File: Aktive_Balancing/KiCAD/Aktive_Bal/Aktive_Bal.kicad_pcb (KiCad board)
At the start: 4 copper layers, 149 x 144 mm, 219 parts, among them J1 Screw_Terminal_01x02, J10 Conn_01x02_Pin, J11 Conn_01x02_Pin, J12 Conn_01x02_Pin, J13 Conn_01x02_Pin, J14 Conn_01x02_Pin, J15 Screw_Terminal_01x03, J16 Screw_Terminal_01x03, J17 Screw_Terminal_01x03, J18 Screw_Terminal_01x03, J19 Screw_Terminal_01x03, J2 A-DF_09_A_KG-T4S, J20 Screw_Terminal_01x03, J21 Conn_01x02_Pin, J22 Conn_01x02_Pin, J23 Conn_01x02_Pin, J24 Conn_01x02_Pin, J3 Conn_01x02_Pin, J4 Conn_01x02_Pin, J5 Conn_01x02_Pin, J6 Conn_01x02_Pin, J7 Sockel_BluePill, J9 Conn_01x02_Pin, Q1 BSS316NH6327XTSA1, Q10_H1 NTTFS6H888NL, Q10_L1 NTTFS6H888NL, Q11_H1 NTTFS6H888NL, Q11_L1 NTTFS6H888NL, Q12_H1 NTTFS6H888NL, Q12_L1 NTTFS6H888NL, Q13_H1 NTTFS6H888NL, Q13_L1 NTTFS6H888NL, Q14_H1 NTTFS6H888NL, Q14_L1 NTTFS6H888NL, Q15_H1 NTTFS6H888NL, Q15_L1 NTTFS6H888NL, Q16_H1 NTTFS6H888NL, Q16_L1 NTTFS6H888NL, Q1_H1 NTTFS6H888NL, Q1_L1 NTTFS6H888NL, Q2_H1 NTTFS6H888NL, Q2_L1 NTTFS6H888NL, Q3_H1 NTTFS6H888NL, Q3_L1 NTTFS6H888NL, Q4_H1 NTTFS6H888NL, Q4_L1 NTTFS6H888NL, Q5_H1 NTTFS6H888NL, Q5_L1 NTTFS6H888NL, Q6_H1 NTTFS6H888NL, Q6_L1 NTTFS6H888NL, Q7_H1 NTTFS6H888NL, Q7_L1 NTTFS6H888NL, Q8_H1 NTTFS6H888NL, Q8_L1 NTTFS6H888NL, Q9_H1 NTTFS6H888NL, Q9_L1 NTTFS6H888NL, U1 RFP12N10L, U10 LTV-847S, U11 LTV-847S, U12 LTV-847S, U13 LTV-847S, U14 TL084, U15 LM2596S-ADJ, U2 ADUM1250ARZ-RL7, U3 SN65HVD233, U4 SCW20C-12, U5 EC1SA16N, U6 PCA9306DC, U7 PCF8575CDB, U8 LM1117MP-3.3, U9 MCP4725xxx-xCH

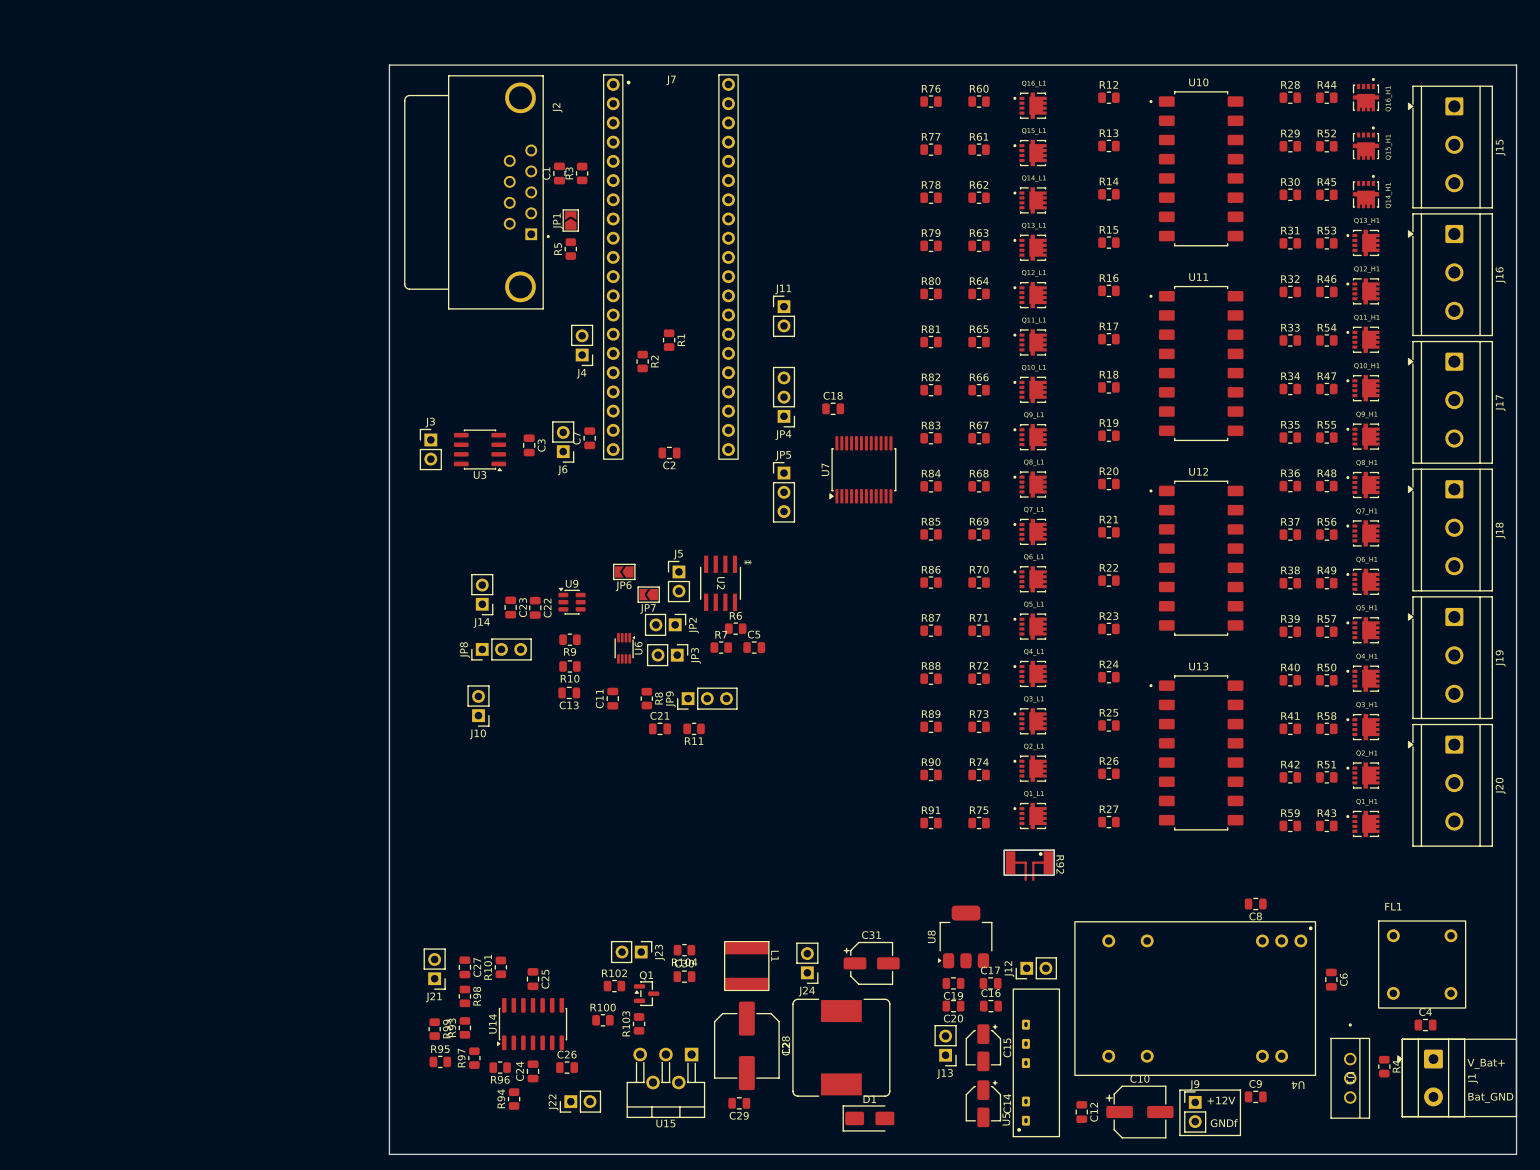
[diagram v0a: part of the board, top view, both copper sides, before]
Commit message: Layout kompakter gemacht
Ich habe die Sektion mit dem Mosfets gemacht. Weber hat es nicht anders gewollt...
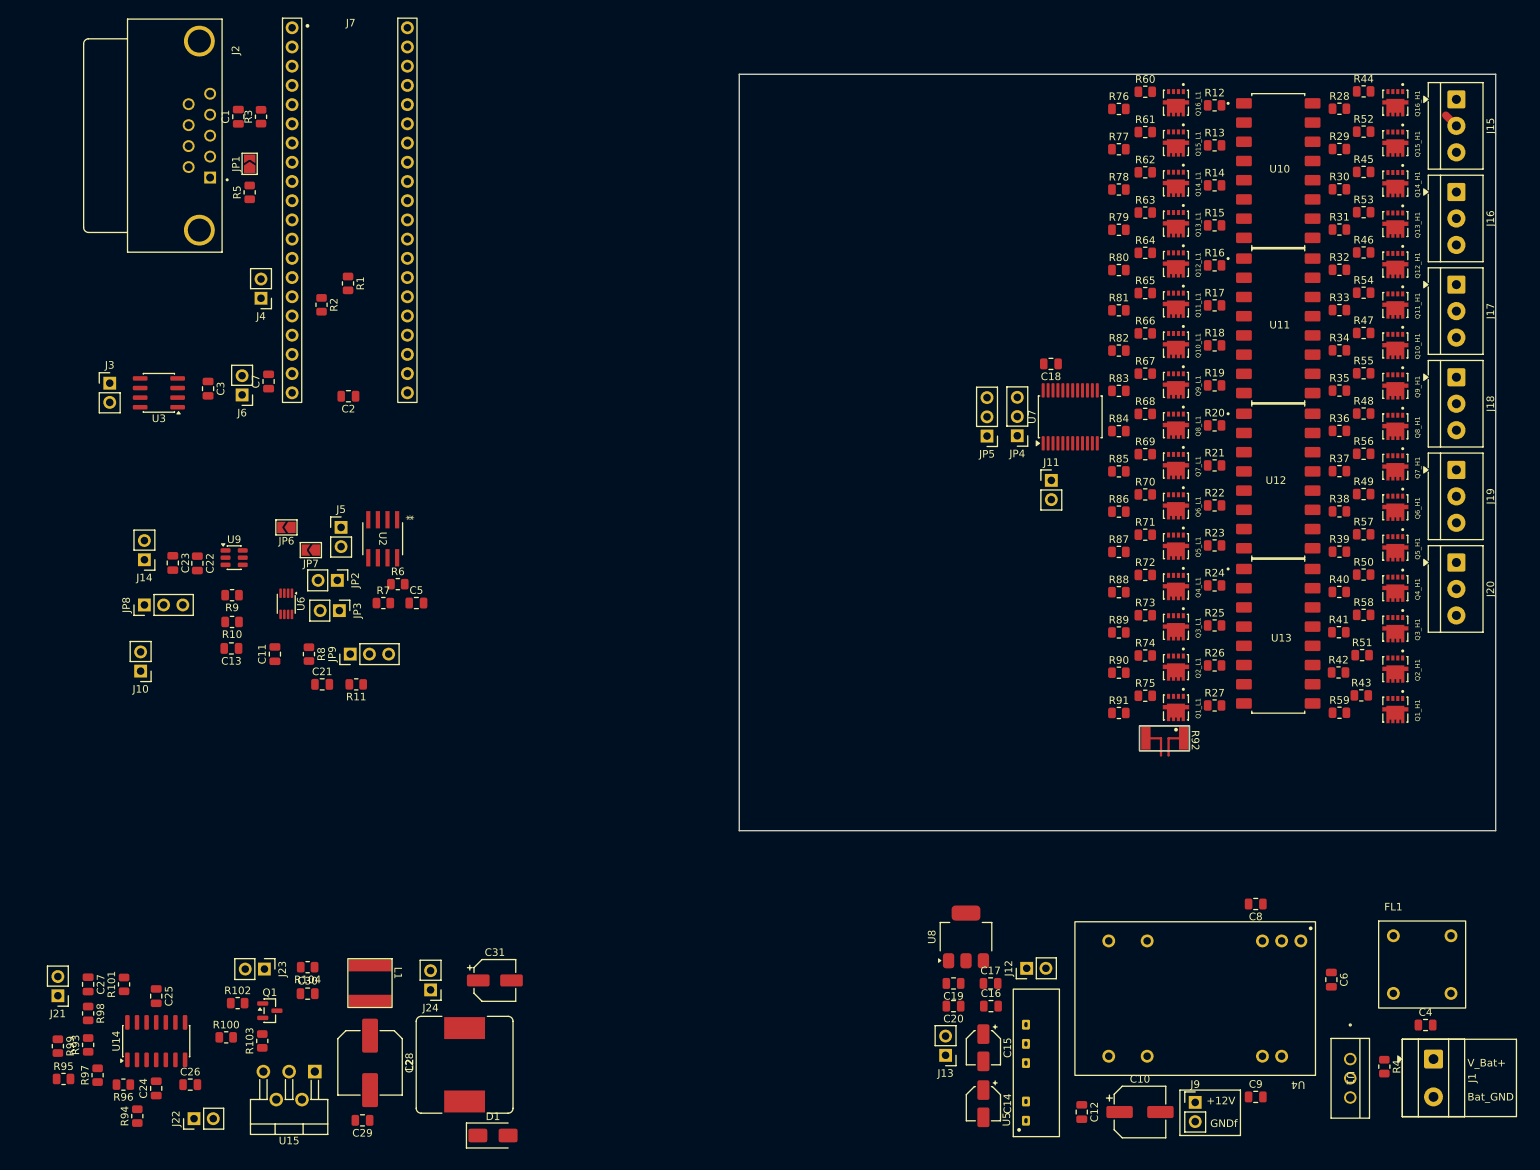
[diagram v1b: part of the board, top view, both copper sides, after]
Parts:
- J15, J16, J17, J18, J19, J20: footprint TerminalBlock_CUI:TerminalBlock_CUI_TB007-508-03_1x03_P5.08mm_Horizontal -> TerminalBlock_4Ucon:TerminalBlock_4Ucon_1x03_P3.50mm_Horizontal
- moved C25 49.9 mm to (59.2, 141.1)
- moved C29 49.9 mm to (86.4, 157.5)
- moved C30 49.9 mm to (79.2, 140.8)
- moved C31 49.9 mm to (103.9, 139.0)
- moved D1 49.9 mm to (103.7, 159.5)
- moved J23 49.9 mm to (73.5, 137.5)
- moved J24 49.9 mm to (95.4, 140.3)
- moved L1 49.9 mm to (87.4, 137.0)
- moved Q1 49.9 mm to (74.2, 143.0)
- moved R102 49.9 mm to (69.9, 142.0)
- moved R103 49.9 mm to (73.2, 147.0)
- moved R104 49.9 mm to (79.2, 137.3)
- moved R94 49.9 mm to (56.7, 156.9)
- moved R99 49.9 mm to (46.2, 147.7)
- moved C24 49.9 mm to (59.2, 153.3)
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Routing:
- net Cell15: track 0.00 -> 1.98 mm
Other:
- board size 149 x 144 mm -> 100 x 100 mm
- board text removed: "Port Expander"

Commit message: hassplatine
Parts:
- moved J10 141.2 mm to (177.0, 23.5)
- moved J14 137.2 mm to (181.0, 23.5)
- moved JP8 131.6 mm to (173.0, 26.0), turned to 180 degrees
- moved C23 127.9 mm to (176.9, 29.0), turned to 180 degrees
- moved C22 123.5 mm to (176.9, 32.5), turned to 180 degrees
- moved R9 117.6 mm to (172.0, 31.0), turned to 90 degrees
- moved U9 116.3 mm to (176.5, 37.5), turned to -90 degrees
- moved R10 116.3 mm to (168.5, 31.0), turned to 90 degrees
- moved C13 115.4 mm to (165.0, 30.9), turned to 90 degrees
- moved J22 113.5 mm to (154.5, 88.5)
- moved U15 110.9 mm to (168.5, 84.0)
- moved JP6 110.2 mm to (179.9, 41.4), turned to 90 degrees
- moved R94 109.9 mm to (143.4, 89.5), turned to 180 degrees
- moved C24 109.5 mm to (146.0, 86.5)
- moved C25 109.5 mm to (146.0, 74.3)
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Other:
- board size 100 x 100 mm -> 108.8 x 101 mm
- board text removed: "+12V"
- board text removed: "Bat_GND"
- board text removed: "CAN-Anbindung mit Sub-D-Stecker, Tranceiver, STM32"
- board text removed: "GNDf"
- board text removed: "I2C-Kram"
- board text removed: "Leistungsmosfets"
- board text removed: "OPV mit Regelkreis"
- board text removed: "Spannungsversorgungen"
- board text removed: "V_Bat+"

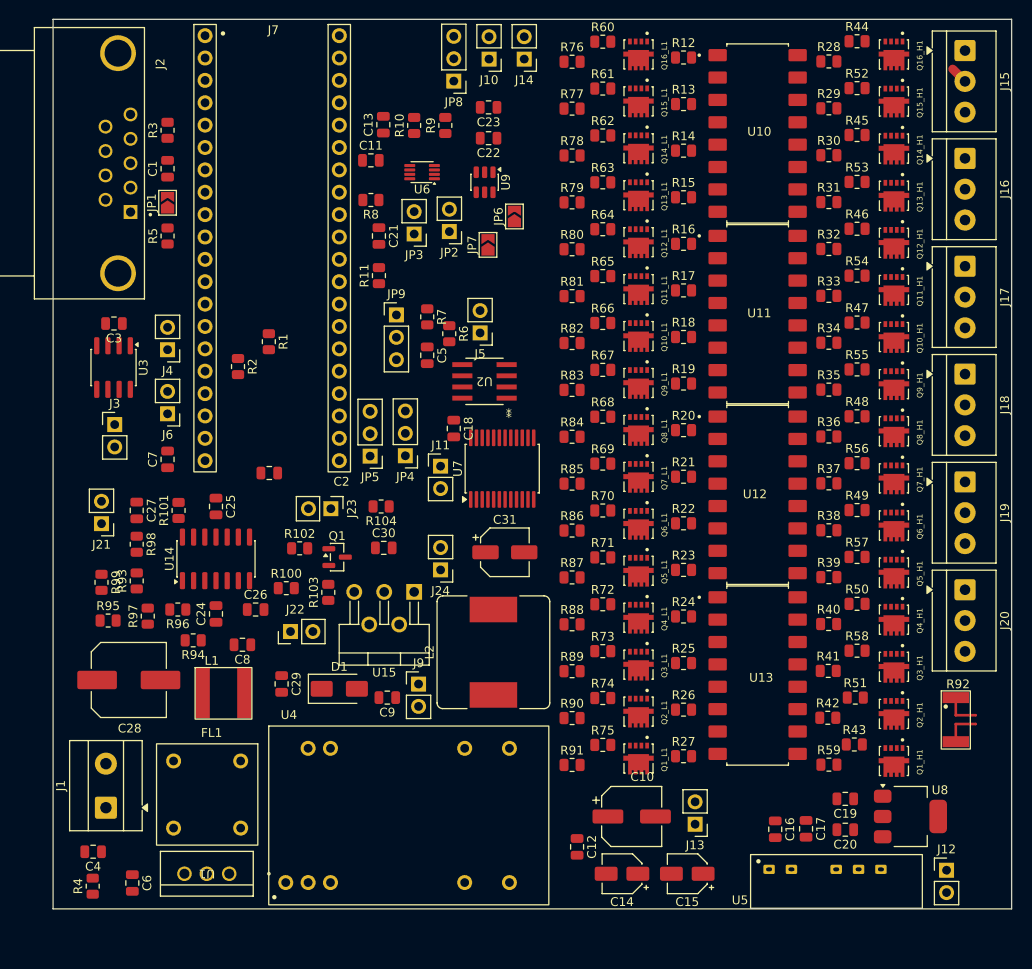
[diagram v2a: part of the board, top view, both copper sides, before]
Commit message: Microcontroller geroutet
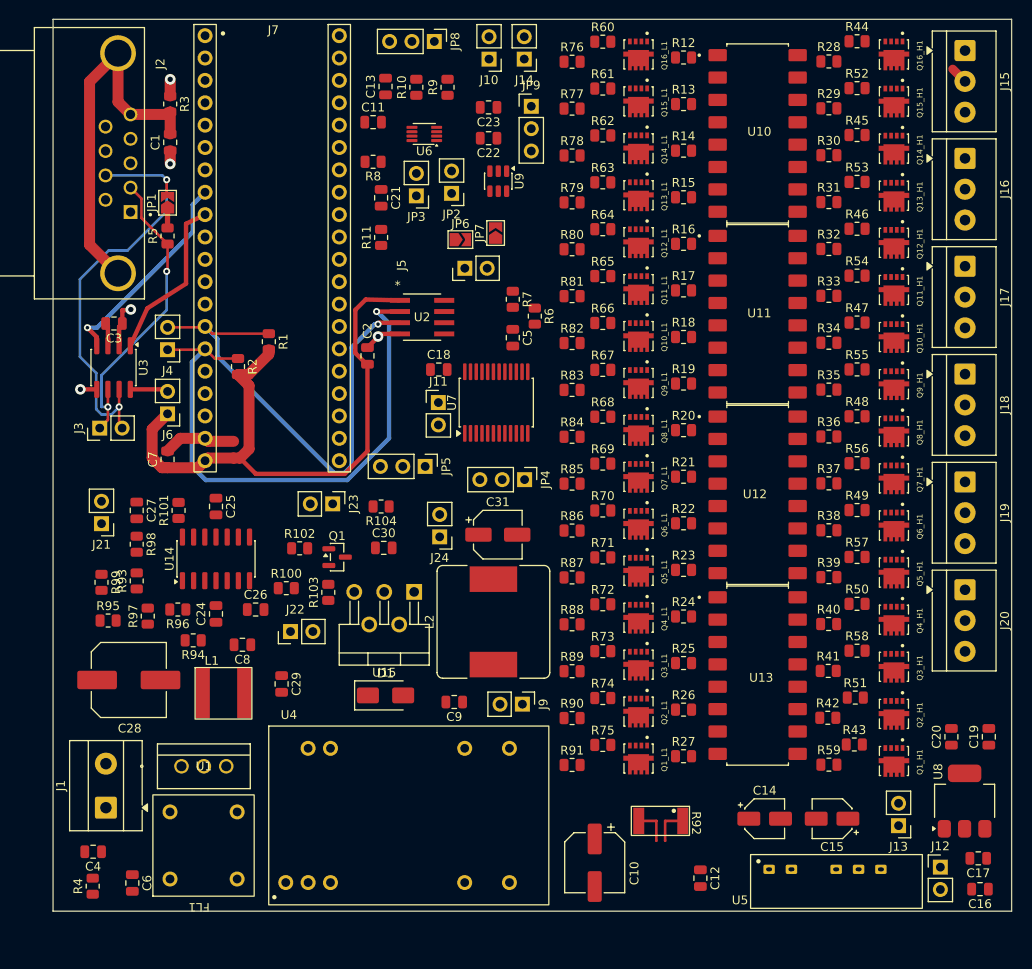
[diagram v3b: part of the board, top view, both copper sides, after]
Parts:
- moved R92 34.0 mm to (199.0, 110.0), turned to -90 degrees
- moved JP9 28.2 mm to (181.8, 28.9)
- moved C16 24.2 mm to (232.8, 117.8), turned to 180 degrees
- moved J13 23.1 mm to (223.5, 110.5)
- moved C17 19.8 mm to (232.6, 114.2), turned to 180 degrees
- moved C19 17.8 mm to (233.8, 100.5), turned to 90 degrees
- moved C15 17.6 mm to (215.9, 109.8)
- moved C14 17.4 mm to (208.3, 109.8), turned to 0 degrees
- moved C2 17.4 mm to (163.2, 57.2), turned to 90 degrees
- moved C20 16.0 mm to (229.5, 100.5), turned to 90 degrees
- moved FL1 15.2 mm to (148.4, 116.6), turned to 90 degrees
- moved C12 14.4 mm to (201.0, 116.5)
- moved JP4 13.8 mm to (181.0, 71.2), turned to -90 degrees
- moved U1 13.4 mm to (142.1, 103.8), turned to 0 degrees
- moved J9 12.0 mm to (180.8, 96.8), turned to -90 degrees
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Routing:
- net +3.3Vµ: track 0.00 -> 73.2 mm
- net SDAµC: track 0.00 -> 65.2 mm, vias 0 -> 1
- net SCLµC: track 0.00 -> 57.0 mm, vias 0 -> 1
- net CANH: track 0.00 -> 49.0 mm, vias 0 -> 2
- net Net-(J2-SHIELD): track 0.00 -> 42.3 mm
- net CANL: track 0.00 -> 35.3 mm, vias 0 -> 2
- net GNDµ: track 0.00 -> 27.5 mm, vias 0 -> 5
- net RX: track 0.00 -> 24.0 mm, vias 0 -> 1
- net TX: track 0.00 -> 19.1 mm
- net Net-(JP1-A): track 0.00 -> 2.14 mm
- added copper zone on In1.Cu, net GNDµ
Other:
- board size 108.8 x 101 mm -> 108.8 x 101.3 mm

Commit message: NEuneuenuenbeuebu
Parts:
- moved JP8 26.5 mm to (181.8, 45.6), turned to 180 degrees
- moved C8 23.8 mm to (151.6, 113.7), turned to -90 degrees
- moved C6 19.3 mm to (151.4, 104.8), turned to 90 degrees
- moved JP9 17.4 mm to (165.8, 22.0), turned to 90 degrees
- moved C13 11.8 mm to (175.8, 31.9), turned to 180 degrees
- moved R6 5.82 mm to (176.9, 50.3), turned to 0 degrees
- moved JP3 4.28 mm to (168.6, 43.3)
- moved C22 4.21 mm to (181.2, 32.7)
- moved C23 4.21 mm to (181.2, 29.2)
- moved R4 4.08 mm to (135.6, 115.5), turned to 180 degrees
- moved R7 3.23 mm to (176.9, 52.4), turned to 0 degrees
- moved C5 2.77 mm to (176.9, 54.8), turned to 180 degrees
- moved D1 2.65 mm to (162.6, 95.7)
- moved C4 1.67 mm to (130.4, 113.8), turned to 90 degrees
- moved C9 1.53 mm to (171.6, 96.8)
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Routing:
- net +3.3V: track 0.00 -> 150.3 mm, vias 0 -> 3
- net +5V: track 0.00 -> 140.9 mm, vias 0 -> 1
- net +12V: track 0.00 -> 54.1 mm
- net GND_float2: track 0.00 -> 46.9 mm, vias 0 -> 15
- net SDA3.3: track 0.00 -> 46.3 mm
- net Net-(C6-Pad1): track 0.00 -> 42.1 mm
- net SCL3.3: track 0.00 -> 42.0 mm, vias 0 -> 2
- net Net-(U1-D): track 0.00 -> 40.0 mm
- net Net-(C6-Pad2): track 0.00 -> 37.3 mm
- net Net-(JP8-B): track 0.00 -> 36.8 mm, vias 0 -> 1
- net SCL5: track 0.00 -> 24.3 mm, vias 0 -> 1
- net BAT+: track 0.00 -> 24.0 mm
- net Net-(JP9-A): track 0.00 -> 22.6 mm, vias 0 -> 1
- net SDA5: track 0.00 -> 21.9 mm
- net -5V: track 0.00 -> 21.5 mm
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- added copper zone on In1.Cu, net Bat_GND

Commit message: beschriftung der pins
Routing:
- net I_Bal: track 0.00 -> 15.1 mm
- net Net-(U14D-+): track 0.00 -> 9.19 mm
- net Net-(U14A-+): track 0.00 -> 9.04 mm
- net Net-(U14D--): track 0.00 -> 5.04 mm
- net Net-(U14C-+): track 0.00 -> 3.95 mm
- net Net-(U14B--): track 0.00 -> 3.69 mm
- net GND_float2: track 46.9 -> 50.4 mm
- net +5V: track 140.9 -> 143.7 mm
- net -5V: track 21.5 -> 24.0 mm
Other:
- board text added: "CANH"
- board text added: "CANL"
- board text added: "SCLµ"
- board text added: "SDAµ"

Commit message: alles neu
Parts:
- moved C29 19.2 mm to (167.6, 81.4), turned to 0 degrees
- moved JP4 17.3 mm to (167.2, 60.9), turned to 0 degrees
- moved J22 15.1 mm to (150.2, 74.0)
- moved D1 7.84 mm to (155.4, 92.6), turned to 180 degrees
- moved R92 4.97 mm to (194.4, 108.1), turned to 90 degrees
- moved L1 3.91 mm to (147.0, 98.5), turned to 90 degrees
- moved R59 3.85 mm to (218.6, 101.2)
- moved R43 3.60 mm to (215.5, 103.3)
- moved C11 1.72 mm to (165.0, 29.4), turned to -90 degrees
- moved C28 1.70 mm to (134.6, 94.8), turned to 180 degrees
- moved J24 1.56 mm to (171.2, 76.2)
- moved R101 1.39 mm to (140.4, 74.4)
- moved R97 1.13 mm to (137.4, 87.5), turned to -90 degrees
- moved R96 0.50 mm to (141.6, 86.5)
- moved R94 0.50 mm to (143.4, 90.0)
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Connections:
- Q10_L1 pad 1: Net-(Q10_L1-S-Pad1) -> V_I_Bal
- Q10_L1 pad 2: Net-(Q10_L1-S-Pad1) -> V_I_Bal
- Q10_L1 pad 3: Net-(Q10_L1-S-Pad1) -> V_I_Bal
- Q11_L1 pad 1: Net-(Q10_L1-S-Pad1) -> V_I_Bal
- Q11_L1 pad 2: Net-(Q10_L1-S-Pad1) -> V_I_Bal
- Q11_L1 pad 3: Net-(Q10_L1-S-Pad1) -> V_I_Bal
- Q12_L1 pad 1: Net-(Q10_L1-S-Pad1) -> V_I_Bal
- Q12_L1 pad 2: Net-(Q10_L1-S-Pad1) -> V_I_Bal
- Q12_L1 pad 3: Net-(Q10_L1-S-Pad1) -> V_I_Bal
- Q13_L1 pad 1: Net-(Q10_L1-S-Pad1) -> V_I_Bal
- Q13_L1 pad 2: Net-(Q10_L1-S-Pad1) -> V_I_Bal
- Q13_L1 pad 3: Net-(Q10_L1-S-Pad1) -> V_I_Bal
- Q14_L1 pad 1: Net-(Q10_L1-S-Pad1) -> V_I_Bal
- Q14_L1 pad 2: Net-(Q10_L1-S-Pad1) -> V_I_Bal
- Q14_L1 pad 3: Net-(Q10_L1-S-Pad1) -> V_I_Bal
- Q15_L1 pad 1: Net-(Q10_L1-S-Pad1) -> V_I_Bal
- Q15_L1 pad 2: Net-(Q10_L1-S-Pad1) -> V_I_Bal
- Q15_L1 pad 3: Net-(Q10_L1-S-Pad1) -> V_I_Bal
- Q16_L1 pad 1: Net-(Q10_L1-S-Pad1) -> V_I_Bal
- Q16_L1 pad 2: Net-(Q10_L1-S-Pad1) -> V_I_Bal
- Q16_L1 pad 3: Net-(Q10_L1-S-Pad1) -> V_I_Bal
- Q1_L1 pad 1: Net-(Q10_L1-S-Pad1) -> V_I_Bal
- Q1_L1 pad 2: Net-(Q10_L1-S-Pad1) -> V_I_Bal
- Q1_L1 pad 3: Net-(Q10_L1-S-Pad1) -> V_I_Bal
- Q2_L1 pad 1: Net-(Q10_L1-S-Pad1) -> V_I_Bal
- Q2_L1 pad 2: Net-(Q10_L1-S-Pad1) -> V_I_Bal
- Q2_L1 pad 3: Net-(Q10_L1-S-Pad1) -> V_I_Bal
- Q3_L1 pad 1: Net-(Q10_L1-S-Pad1) -> V_I_Bal
- Q3_L1 pad 2: Net-(Q10_L1-S-Pad1) -> V_I_Bal
- Q3_L1 pad 3: Net-(Q10_L1-S-Pad1) -> V_I_Bal
- Q4_L1 pad 1: Net-(Q10_L1-S-Pad1) -> V_I_Bal
- Q4_L1 pad 2: Net-(Q10_L1-S-Pad1) -> V_I_Bal
- Q4_L1 pad 3: Net-(Q10_L1-S-Pad1) -> V_I_Bal
- Q5_L1 pad 1: Net-(Q10_L1-S-Pad1) -> V_I_Bal
- Q5_L1 pad 2: Net-(Q10_L1-S-Pad1) -> V_I_Bal
- Q5_L1 pad 3: Net-(Q10_L1-S-Pad1) -> V_I_Bal
- Q6_L1 pad 1: Net-(Q10_L1-S-Pad1) -> V_I_Bal
- Q6_L1 pad 2: Net-(Q10_L1-S-Pad1) -> V_I_Bal
- Q6_L1 pad 3: Net-(Q10_L1-S-Pad1) -> V_I_Bal
- Q7_L1 pad 1: Net-(Q10_L1-S-Pad1) -> V_I_Bal
- Q7_L1 pad 2: Net-(Q10_L1-S-Pad1) -> V_I_Bal
- Q7_L1 pad 3: Net-(Q10_L1-S-Pad1) -> V_I_Bal
- Q8_L1 pad 1: Net-(Q10_L1-S-Pad1) -> V_I_Bal
- Q8_L1 pad 2: Net-(Q10_L1-S-Pad1) -> V_I_Bal
- Q8_L1 pad 3: Net-(Q10_L1-S-Pad1) -> V_I_Bal
- Q9_L1 pad 1: Net-(Q10_L1-S-Pad1) -> V_I_Bal
- Q9_L1 pad 2: Net-(Q10_L1-S-Pad1) -> V_I_Bal
- Q9_L1 pad 3: Net-(Q10_L1-S-Pad1) -> V_I_Bal
- R92 pad 1: Net-(Q10_L1-S-Pad1) -> V_I_Bal
- R92 pad 2: V_I_Bal -> GND_float2
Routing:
- net GND_float2: track 50.4 -> 279.9 mm, vias 15 -> 56
- net V_I_Bal: track 0.00 -> 223.7 mm, vias 0 -> 2
- net Bal: track 0.00 -> 197.7 mm, vias 0 -> 17
- net +12V: track 54.1 -> 225.1 mm, vias 0 -> 3
- net -5V: track 24.0 -> 156.6 mm, vias 0 -> 1
- net +5V: track 143.7 -> 245.9 mm, vias 1 -> 3
- net Cell1: track 0.00 -> 73.0 mm, vias 0 -> 1
- net Cell2: track 0.00 -> 71.5 mm, vias 0 -> 1
- net I_Bal_Soll: track 16.1 -> 87.3 mm, vias 1 -> 2
- net B1: track 0.00 -> 70.2 mm, vias 0 -> 3
- net Cell3: track 0.00 -> 69.1 mm, vias 0 -> 1
- net Cell5: track 0.00 -> 67.2 mm, vias 0 -> 1
- net Cell4: track 0.00 -> 66.1 mm, vias 0 -> 1
- net Cell6: track 0.00 -> 63.9 mm, vias 0 -> 1
- net Cell7: track 0.00 -> 60.7 mm, vias 0 -> 1
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- added copper zone on In1.Cu, net GND_float2

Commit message: opto verschobnen und krams
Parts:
- moved U10 1.52 mm to (207.5, 30.4)
- moved U13 1.52 mm to (207.5, 95.0)
- moved U11 0.51 mm to (207.5, 52.0)
- moved U12 0.51 mm to (207.5, 73.5)
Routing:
- net GND_float2: track 279.9 -> 298.4 mm, vias 56 -> 53
- net +12V: track 225.1 -> 232.0 mm, vias 3 -> 2
- net GNDµ: track 27.5 -> 24.1 mm
- net +3.3V: track 186.7 -> 183.9 mm, vias 3 -> 2
- net Net-(R27-Pad2): track 4.53 -> 3.49 mm
- net Net-(R14-Pad2): track 3.24 -> 3.87 mm
- net Net-(R13-Pad2): track 3.16 -> 3.79 mm
- net Net-(R12-Pad2): track 3.07 -> 3.70 mm
- net Net-(R26-Pad2): track 4.04 -> 3.40 mm
- net Net-(R24-Pad2): track 3.86 -> 3.23 mm
- net Net-(R28-Pad1): track 3.39 -> 2.76 mm
- net Net-(R25-Pad2): track 3.95 -> 3.32 mm
- net Net-(R15-Pad2): track 3.33 -> 3.96 mm
- net Net-(R29-Pad1): track 3.29 -> 2.66 mm
- net Net-(R36-Pad1): track 2.75 -> 3.35 mm
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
